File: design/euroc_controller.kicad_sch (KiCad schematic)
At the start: 63 parts, among them J1 xt30, J2 jst_sh 4, J4 jst_sh 4, J5 jst_sh 4, J6 SMA, J8 USB_C_Receptacle_USB2.0, J9 jst_sh 4, Q1 MMBT3904, U1 TPSM5601R5, U13 STM32U575CGTx, U2 USBLC6-2SC6, U3 LSM6DSO32, U4 MS5611-01BA, U5 SN65HVD232, U6 W25Q128JVS, U7 RFM69W, U8 L86, Y1 48MHz

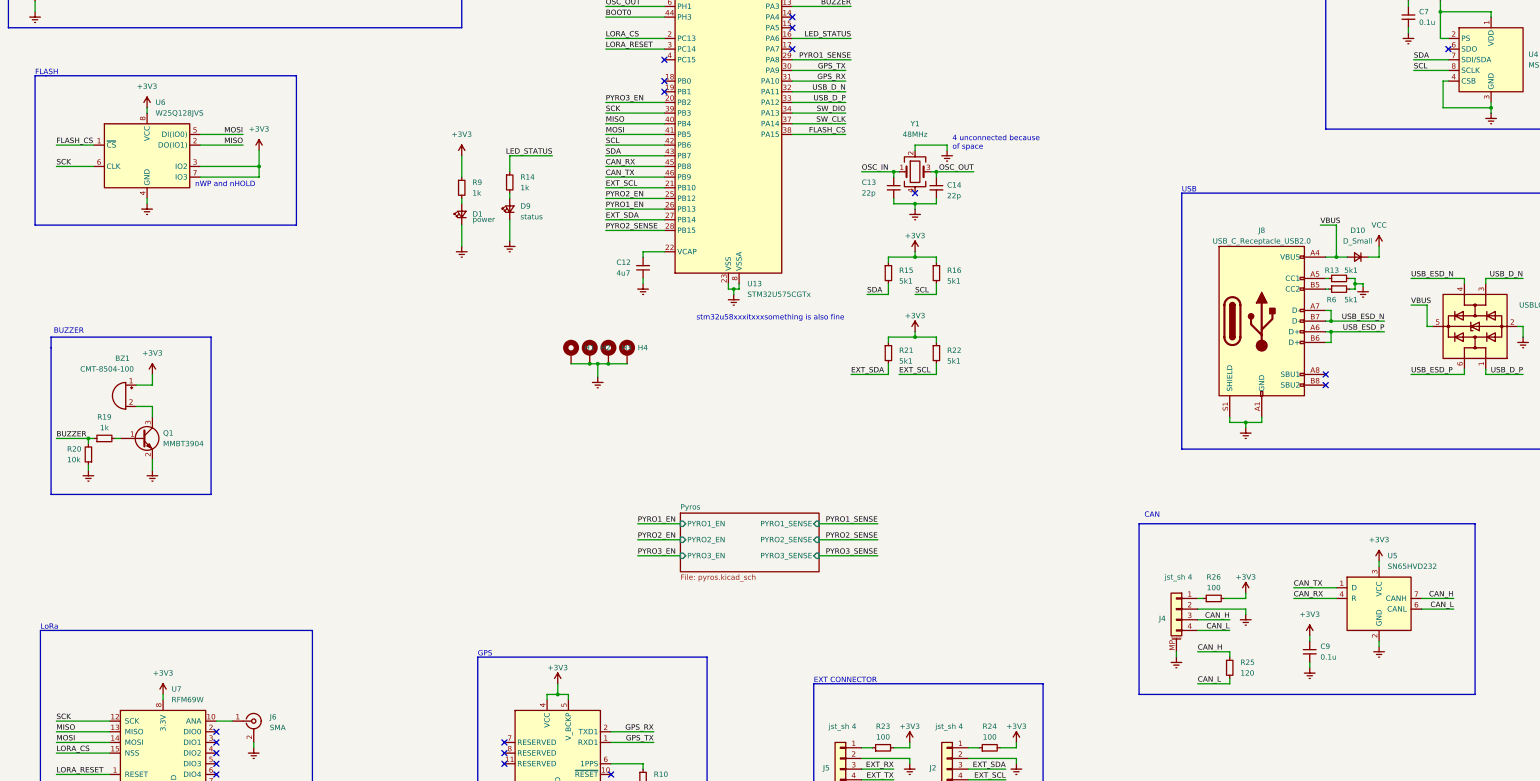
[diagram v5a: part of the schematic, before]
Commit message: can transceiver, decoupling caps
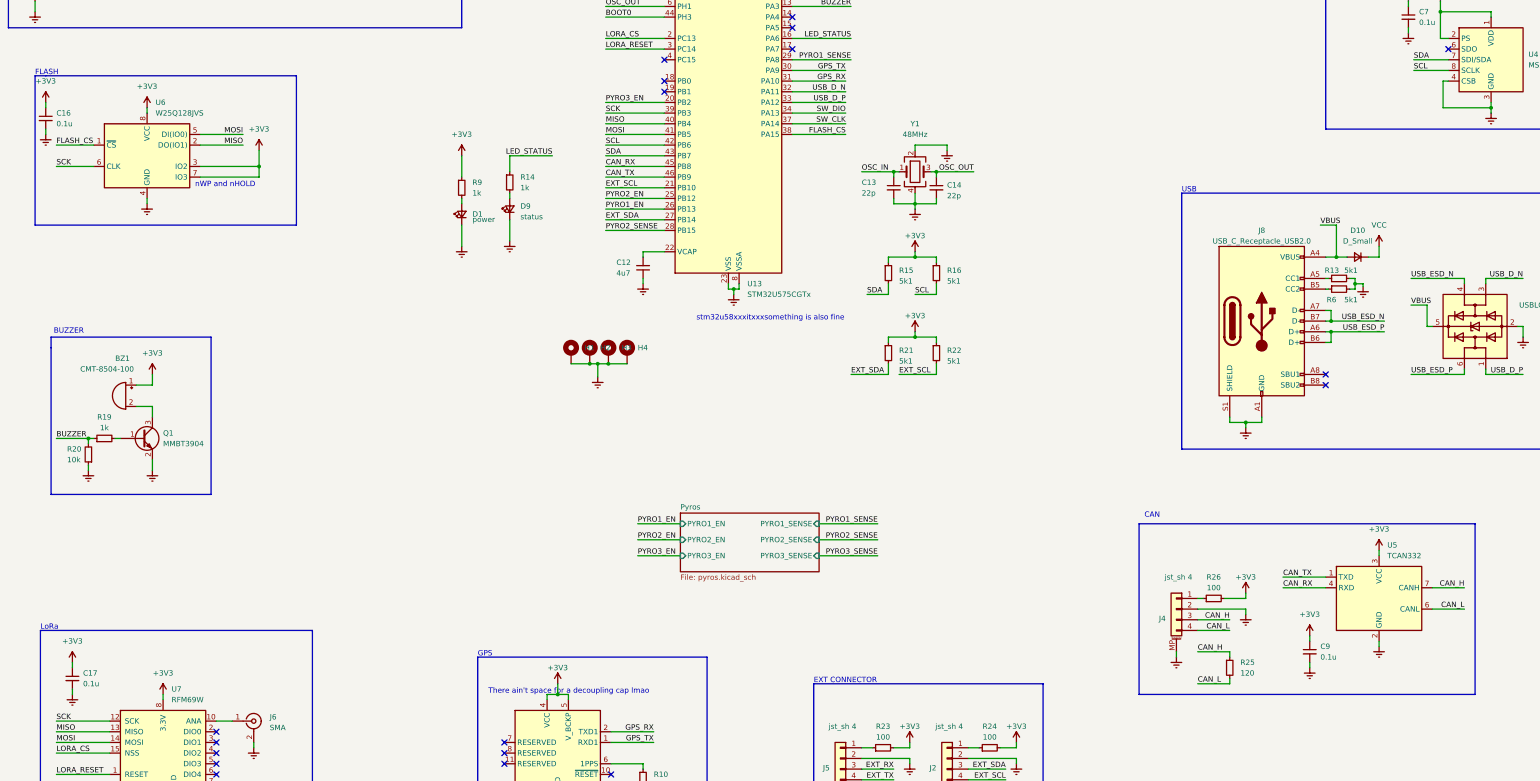
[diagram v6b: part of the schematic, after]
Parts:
- added C16, C17: 0.1u, Capacitor_SMD:C_0603_1608Metric, symbol Device:C_Small
- U5: value SN65HVD232 -> TCAN332; symbol Interface_CAN_LIN:SN65HVD232 -> Interface_CAN_LIN:TCAN332
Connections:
- net +3V3: now also C16.1, C17.1
- net Earth: now also Y1.4, C16.2, C17.2
- no-connect marks 24 -> 23
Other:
- note added: "There ain't space for a decoupling cap lmao"
- note removed: "4 unconnected because of space"
- moved on the sheet: U5

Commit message: fix aesir logo
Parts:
- U1: footprint Package_DFN_QFN:Texas_B3QFN-14-1EP_5x5.5mm_P0.65mm_ThermalVia -> Package_DFN_QFN:Texas_B3QFN-14-1EP_5x5.5mm_P0.65mm
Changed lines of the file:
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@@
       (effects (font (size 1.27 1.27)))
     )
-    (property "Footprint" "Package_DFN_QFN:Texas_B3QFN-14-1EP_5x5.5mm_P0.65mm_ThermalVia" (at 60.96 33.02 0)
+    (property "Footprint" "Package_DFN_QFN:Texas_B3QFN-14-1EP_5x5.5mm_P0.65mm" (at 60.96 33.02 0)
       (effects (font (size 1.27 1.27)) (justify left) hide)
     )

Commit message: better sma
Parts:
- J6: footprint Connector_Coaxial:SMA_Molex_73251-1153_EdgeMount_Horizontal -> Connector_Coaxial:SMA_Amphenol_901-143_Horizontal
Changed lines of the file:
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@@
       (effects (font (size 1.27 1.27)) (justify left))
     )
-    (property "Footprint" "Connector_Coaxial:SMA_Molex_73251-1153_EdgeMount_Horizontal" (at 71.12 250.19 0)
+    (property "Footprint" "Connector_Coaxial:SMA_Amphenol_901-143_Horizontal" (at 71.12 250.19 0)
       (effects (font (size 1.27 1.27)) hide)
     )
